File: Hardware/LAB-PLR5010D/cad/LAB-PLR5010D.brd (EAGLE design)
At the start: 44.5 x 29.2 mm, 8 parts, among them J2 22-23-2021, J3 22-23-2021, U1 DAC8562, U2 LT3080, U3 LT3080

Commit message: 1) Committing final Rev0 of the PLR5010
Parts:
- removed J3: 22-23-2021, My Library-adm:22-23-2021
- added C3, C4: 33nf, SparkFun-Capacitors:0603-CAP
- J2: value 22-23-2021 -> 1729021; device My Library-adm:22-23-2021 -> My Library-adm:1729021
- moved J2 27.4 mm to (22.2, 27.6)
- moved C1 24.2 mm to (22.2, 8.26)
- moved C2 24.2 mm to (22.2, 6.03)
- moved J1 24.2 mm to (22.2, 3.81)
- moved U1 24.2 mm to (22.2, 10.8)
- moved U2 24.1 mm to (10.2, 18.1)
- moved U3 24.1 mm to (34.3, 18.1)
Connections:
- net GND: now also C3.2, C4.2, J2.P$2; no longer J2.2, J3.1
- net N$2: now also C3.1
- net N$3: now also C4.1
- net VA: now also J2.P$1; no longer J2.1
- net VB: now also J2.P$3; no longer J3.2
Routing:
- net GND: track 8.18 -> 29.4 mm, vias 0 -> 2
- net VDDIO: track 52.7 -> 38.8 mm, vias 1 -> 3
- net VA: track 0.00 -> 8.76 mm, vias 156 -> 173
- net VDDLDO: track 41.0 -> 37.3 mm, vias 4 -> 2
- net VB: track 0.00 -> 3.37 mm, vias 160 -> 173
- net N$2: track 15.7 -> 18.1 mm
- net N$3: track 14.8 -> 16.0 mm
- removed copper zone on layer 16, net GND
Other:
- board size 44.5 x 29.2 mm -> 44.5 x 31.8 mm
- board text added: "!CLR"
- board text added: "!CS"
- board text added: "!LDAC"
- board text added: "GND"
- board text added: "LAB-PLR5010D"
- board text added: "MCLK"
- board text added: "MOSI"
- board text added: "VA"
- board text added: "VB"
- board text added: "VDDIO"
- board text added: "VDDLDO"

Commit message: 1) Checkpoint before cleanup, final BOM and MFG
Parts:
- removed U2, U3: LT3080, LAB-PLR1010:DDPAK5(Q)
- added Q1, Q2: FZT849, LAB304:SOT223
- added R1, R2: (no value), rcl:R0603
- J1: device con-lstb:MA10-1W -> con-lstb:MA04-1
- J2: value 1729021 -> (none); device My Library-adm:1729021 -> con-lstb:MA04-1
- moved C3 20.8 mm to (3.81, 2.86), flipped to the bottom, turned to 270 degrees
- moved J2 20.8 mm to (12.1, 9.53)
- moved C4 11.5 mm to (20.3, 3.17), flipped to the bottom
- moved U1 11.4 mm to (12.1, 5.71)
- moved J1 10.3 mm to (12.1, 1.91), flipped to the top, turned to 0 degrees
- moved C1 7.67 mm to (14.7, 6.83), flipped to the bottom
- moved C2 7.65 mm to (14.7, 4.76), flipped to the bottom
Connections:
- removed net N$2: C3.1, U1.1, U2.2
- removed net VA: J1.1, J2.P$1, U2.3, U2.TAB
- removed net VB: J1.10, J2.P$3, U3.3, U3.TAB
- new net N$1: C3.1, R1.1, U1.1
- new net N$4: Q1.1, R1.2
- new net N$5: Q2.1, R2.2
- net !CLR: now also J1.2; no longer J1.3
- net !CS: now also J1.3; no longer J1.7
- net !LDAC: now also J1.1; no longer J1.2
- net GND: now also J2.1, Q1.3, Q2.3; no longer J1.5, J2.P$2
- net MCLK: now also J1.4; no longer J1.8
- net MOSI: now also J2.2; no longer J1.9
- net N$3: now also R2.1; no longer U3.2
- net VDDIO: now also J2.3; no longer J1.6, U2.4, U3.4
- net VDDLDO: now also J2.4, Q1.2, Q1.4, Q2.2, Q2.4; no longer J1.4, U2.5, U3.5
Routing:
- net VDDLDO: track 37.3 -> 3.31 mm, vias 2 -> 0
- net VDDIO: track 38.8 -> 9.11 mm, vias 3 -> 1
- net N$2: track 18.1 -> 0.00 mm
- net GND: track 29.4 -> 11.5 mm
- net N$1: track 0.00 -> 9.69 mm, vias 0 -> 1
- net VA: track 8.76 -> 0.00 mm, vias 173 -> 0
- net !LDAC: track 9.93 -> 4.37 mm
- net !CLR: track 8.02 -> 3.16 mm
- net MCLK: track 8.60 -> 4.37 mm
- net N$3: track 16.0 -> 12.2 mm, vias 0 -> 1
- net N$5: track 0.00 -> 3.75 mm, vias 0 -> 1
- net MOSI: track 10.3 -> 6.79 mm, vias 0 -> 1
- net !CS: track 6.69 -> 3.16 mm
- net VB: track 3.37 -> 0.00 mm, vias 173 -> 0
- net N$4: track 0.00 -> 3.22 mm, vias 0 -> 1
- added copper zone on layer 16, net GND
- added copper zone on layer 1, net VDDLDO
- removed copper zone on layer 1, net VA
- removed copper zone on layer 16, net VA
- removed copper zone on layer 1, net VB
- removed copper zone on layer 16, net VB
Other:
- board size 44.5 x 31.8 mm -> 24.1 x 11.4 mm
- board text added: "LAB-PLR"
- board text added: "PLR5010D"
- board text added: "VLDO"
- board text removed: "LAB-PLR5010D"
- board text removed: "VA"
- board text removed: "VB"
- board text removed: "VDDLDO"

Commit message: 1) Releasing new revision for MFG
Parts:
- R1, R2: value (none) -> 390R
- U1: device LAB-PLR1010:MSOP10 -> LAB-PLR5010D:MSOP10
- moved C3 3.89 mm to (3.81, 6.75), turned to 0 degrees
- moved C4 3.55 mm to (18.0, 5.87)
- moved R1 2.94 mm to (3.81, 4.68), turned to 0 degrees
- moved C1 2.88 mm to (11.8, 7.22), turned to 0 degrees
- moved C2 2.88 mm to (11.8, 5.16), turned to 0 degrees
- moved R2 0.32 mm to (18.0, 2.86), turned to 270 degrees
- moved U1 0.32 mm to (12.1, 5.40)
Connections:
- removed net !LDAC: J1.1, U1.4
- removed net VDDIO: C1.1, C2.1, J2.3, U1.9
- removed net VDDLDO: J2.4, Q1.2, Q1.4, Q2.2, Q2.4, U1.10
- new net CHA: J2.1, Q1.2, Q1.4
- new net CHB: J2.4, Q2.2, Q2.4
- new net VDD: C1.1, C2.1, J2.3, U1.10, U1.9
- net GND: now also J1.1, U1.4; no longer J2.1
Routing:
- net VDD: track 0.00 -> 9.15 mm
- net VDDIO: track 9.11 -> 0.00 mm, vias 1 -> 0
- net !LDAC: track 4.37 -> 0.00 mm
- net VDDLDO: track 3.31 -> 0.00 mm
- net GND: track 11.5 -> 8.89 mm
- net N$1: track 9.69 -> 7.64 mm
- net N$3: track 12.2 -> 10.3 mm
- net N$4: track 3.22 -> 4.77 mm
- net N$5: track 3.75 -> 2.88 mm
- net MOSI: track 6.79 -> 5.98 mm, vias 1 -> 0
- added copper zone on layer 1, net CHA
- added copper zone on layer 1, net CHB
- removed copper zone on layer 1, net VDDLDO
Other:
- board text added: "CHA"
- board text added: "CHB"
- board text added: "VDD"
- board text removed: "!LDAC"
- board text removed: "VDDIO"
- board text removed: "VLDO"

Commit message: 1) Updating the BOMs to include pricing and unifying passive MFG sources (samsung resistors).
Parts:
- C3, C4: value 33nf -> 0.01uF
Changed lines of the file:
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@@
 <?xml version="1.0" encoding="utf-8"?>
 <!DOCTYPE eagle SYSTEM "eagle.dtd">
-<eagle version="6.6.0">
+<eagle version="7.3.0">
 <drawing>
 <settings>
@@
 <pass name="Default">
 <param name="RoutingGrid" value="50mil"/>
+<param name="AutoGrid" value="1"/>
+<param name="Efforts" value="0"/>
+<param name="TopRouterVariant" value="1"/>
 <param name="tpViaShape" value="round"/>
 <param name="PrefDir.1" value="|"/>
@@
 <attribute name="VALUE" x="12.842875" y="6.080125" size="0.4064" layer="28" font="vector" rot="MR0"/>
 </element>
-<element name="C3" library="SparkFun-Capacitors" package="0603-CAP" value="33nf" x="3.81" y="6.746875" smashed="yes" rot="MR0">
+<element name="C3" library="SparkFun-Capacitors" package="0603-CAP" value="0.01uF" x="3.81" y="6.746875" smashed="yes" rot="MR0">
 <attribute name="PROD_ID" value="CAP-07886" x="3.81" y="6.746875" size="1.778" layer="28" rot="MR0" display="off"/>
 <attribute name="NAME" x="2.8575" y="8.73125" size="1.016" layer="26" font="vector" rot="MR180"/>
 <attribute name="VALUE" x="4.826" y="5.603875" size="0.4064" layer="28" font="vector" rot="MR0"/>
 </element>
-<element name="C4" library="SparkFun-Capacitors" package="0603-CAP" value="33nf" x="18.018125" y="5.87375" smashed="yes" rot="MR90">
+<element name="C4" library="SparkFun-Capacitors" package="0603-CAP" value="0.01uF" x="18.018125" y="5.87375" smashed="yes" rot="MR90">
 <attribute name="PROD_ID" value="CAP-07886" x="18.018125" y="5.87375" size="1.778" layer="28" rot="MR90" display="off"/>
 <attribute name="NAME" x="19.129375" y="5.000625" size="1.016" layer="26" font="vector" rot="MR90"/>

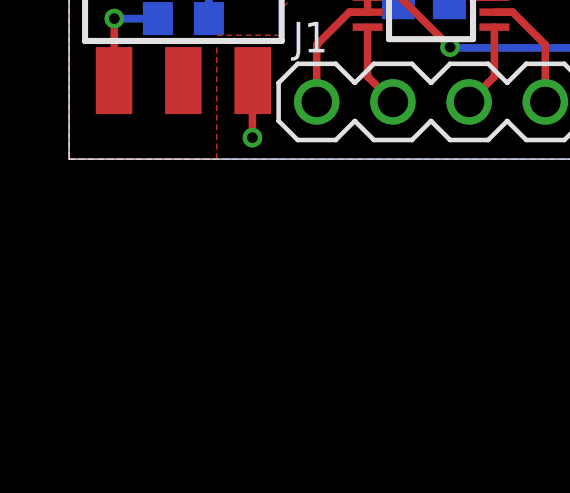
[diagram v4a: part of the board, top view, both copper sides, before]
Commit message: 1) Updating the PLR-5010D as-built 2) Adding the linearization xls
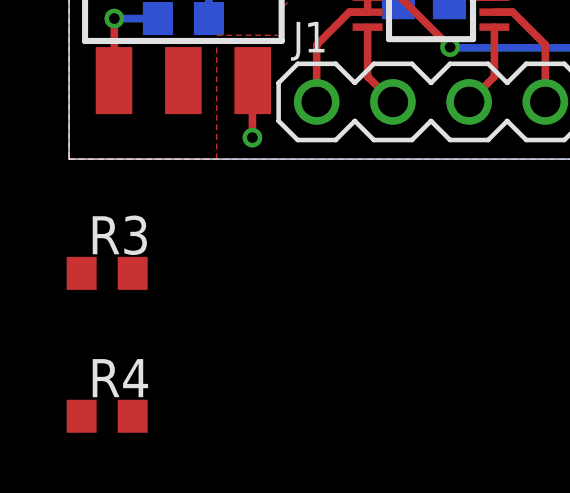
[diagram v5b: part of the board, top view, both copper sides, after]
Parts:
- added R3, R4: 27K, rcl:R0603
- R1, R2: value 390R -> 3.9K
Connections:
- net CHA: now also R3.2
- net CHB: now also R4.2
- net N$4: now also R3.1
- net N$5: now also R4.1
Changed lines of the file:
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@@
 <?xml version="1.0" encoding="utf-8"?>
 <!DOCTYPE eagle SYSTEM "eagle.dtd">
-<eagle version="7.3.0">
+<eagle version="6.6.0">
 <drawing>
 <settings>
@@
 <pass name="Default">
 <param name="RoutingGrid" value="50mil"/>
-<param name="AutoGrid" value="1"/>
-<param name="Efforts" value="0"/>
-<param name="TopRouterVariant" value="1"/>
 <param name="tpViaShape" value="round"/>
 <param name="PrefDir.1" value="|"/>
@@
 <attribute name="VALUE" x="17.78" y="4.3942" size="1.27" layer="27"/>
 </element>
-<element name="R1" library="rcl" package="R0603" value="390R" x="3.81" y="4.683125" smashed="yes" rot="MR0">
+<element name="R1" library="rcl" package="R0603" value="3.9K" x="3.81" y="4.683125" smashed="yes" rot="MR0">
 <attribute name="NAME" x="2.8575" y="3.730625" size="1.016" layer="26" rot="MR180"/>
 <attribute name="VALUE" x="4.445" y="2.778125" size="1.27" layer="28" rot="MR0"/>
 </element>
-<element name="R2" library="rcl" package="R0603" value="390R" x="18.018125" y="2.8575" smashed="yes" rot="MR270">
+<element name="R2" library="rcl" package="R0603" value="3.9K" x="18.018125" y="2.8575" smashed="yes" rot="MR270">
 <attribute name="NAME" x="20.081875" y="3.81" size="1.016" layer="26" rot="MR270"/>
 <attribute name="VALUE" x="19.923125" y="3.4925" size="1.27" layer="28" rot="MR270"/>
@@
 <attribute name="VALUE" x="9.525" y="2.0955" size="1.27" layer="27" ratio="10"/>
 </element>
+<element name="R3" library="rcl" package="R0603" value="27K" x="1.27" y="-3.81"/>
+<element name="R4" library="rcl" package="R0603" value="27K" x="1.27" y="-8.5725"/>
 </elements>
 <signals>
@@
 <wire x1="1.508125" y1="4.683125" x2="2.96" y2="4.683125" width="0.254" layer="16"/>
 <wire x1="1.4986" y1="1.9939" x2="1.508125" y2="2.003425" width="0.254" layer="1"/>
+<contactref element="R3" pad="1"/>
+<wire x1="1.4986" y1="1.9939" x2="0.42" y2="-3.81" width="0" layer="19" extent="1-1"/>
 </signal>
 <signal name="N$5">
@@
 <wire x1="18.018125" y1="0.873125" x2="18.0086" y2="0.88265" width="0.254" layer="1"/>
 <wire x1="18.0086" y1="0.88265" x2="18.0086" y2="2.6162" width="0.254" layer="1"/>
+<contactref element="R4" pad="1"/>
+<wire x1="0.42" y1="-8.5725" x2="18.018125" y2="0.873125" width="0" layer="19" extent="1-16"/>
 </signal>
 <signal name="CHA">
@@
 <vertex x="9.525" y="7.46125"/>
 </polygon>
+<contactref element="R3" pad="2"/>
+<wire x1="3.81" y1="2.6162" x2="2.12" y2="-3.81" width="0" layer="19" extent="1-1"/>
 </signal>
 <signal name="CHB">
@@
 <vertex x="14.605" y="7.46125"/>
 </polygon>
+<contactref element="R4" pad="2"/>
+<wire x1="20.32" y1="2.6162" x2="2.12" y2="-8.5725" width="0" layer="19" extent="1-1"/>
 </signal>
 <signal name="VDD">
